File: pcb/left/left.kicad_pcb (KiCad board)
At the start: 2 copper layers, 30.5 x 66 mm, 21 parts

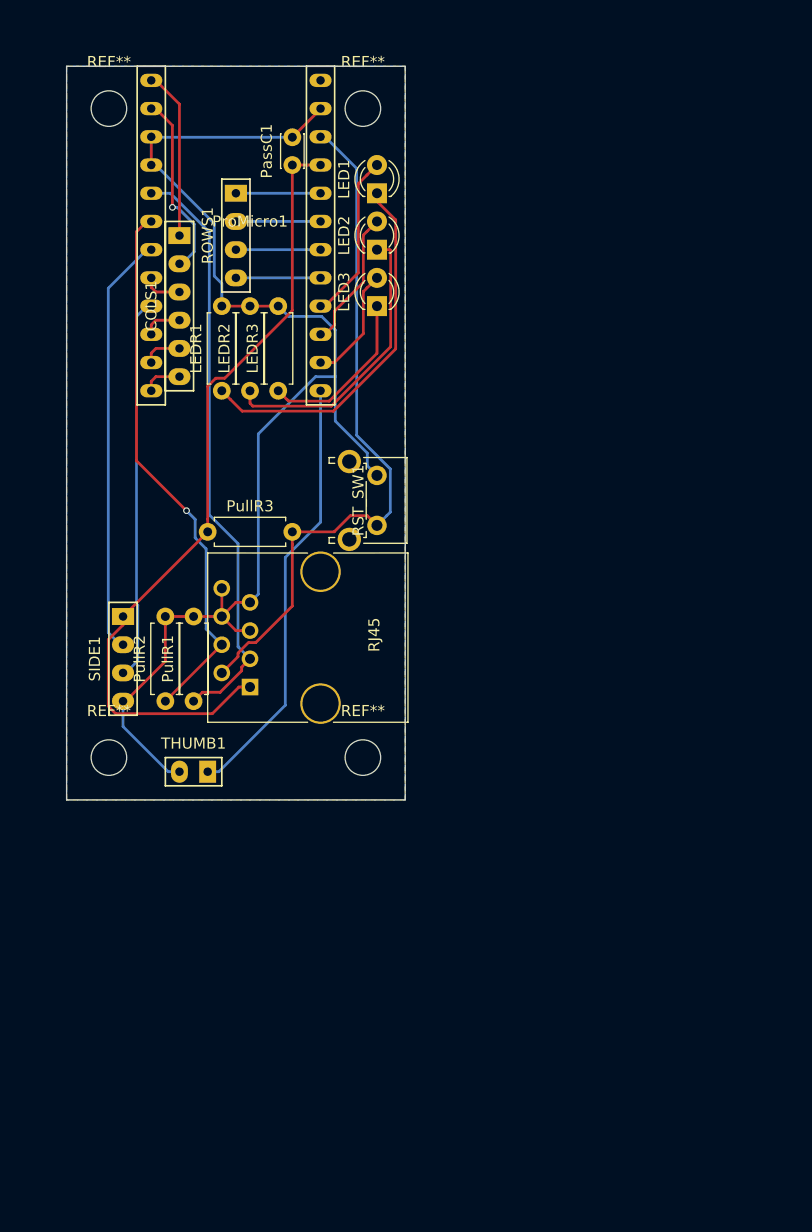
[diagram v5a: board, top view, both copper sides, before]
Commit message: improve parts arrangement
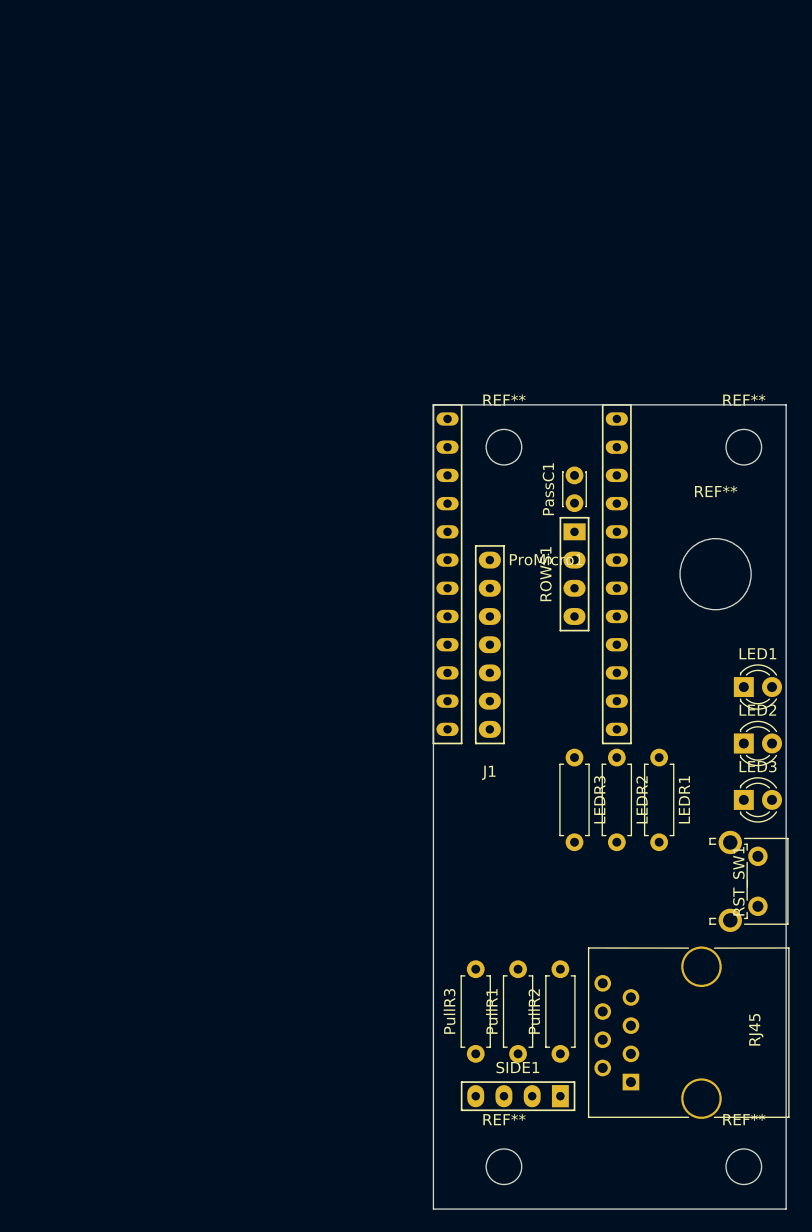
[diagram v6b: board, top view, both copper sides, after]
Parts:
- removed COLS1: Conn_01x06, 4x6t2:Wirepad_01x06
- removed the REF** at (2.54, 2.54)
- removed the REF** at (25.4, 2.54)
- removed the REF** at (2.54, 61.0)
- removed the REF** at (25.4, 61.0)
- removed THUMB1: Conn_01x02, 4x6t2:Wirepad_01x02
- added J1: Conn_01x07, 4x6t2:Wirepad_01x07, F.Cu at (36.8, 57.1)
- added REF**: MountingHole_3.2mm_M3, Mounting_Holes:MountingHole_3.2mm_M3, F.Cu at (59.7, 33.0)
- added REF**: MountingHole_6.4mm_M6, Mounting_Holes:MountingHole_6.4mm_M6, F.Cu at (57.1, 44.5)
- added REF**: MountingHole_3.2mm_M3, Mounting_Holes:MountingHole_3.2mm_M3, F.Cu at (59.7, 97.8)
- added REF**: MountingHole_3.2mm_M3, Mounting_Holes:MountingHole_3.2mm_M3, F.Cu at (38.1, 33.0)
- added REF**: MountingHole_3.2mm_M3, Mounting_Holes:MountingHole_3.2mm_M3, F.Cu at (38.1, 97.8)
- moved LED1 55.4 mm to (59.7, 54.6), turned to 0 degrees
- moved LED2 55.4 mm to (59.7, 59.7), turned to 0 degrees
- moved LED3 55.4 mm to (59.7, 64.8), turned to 0 degrees
- moved SIDE1 53.1 mm to (39.4, 91.4), turned to 270 degrees
- moved PullR3 52.8 mm to (35.6, 87.6), turned to 90 degrees
- moved LEDR1 51.4 mm to (52.1, 61.0), turned to 270 degrees
- moved RJ45 49.4 mm to (49.5, 90.2)
- moved RST_SW1 48.5 mm to (61.0, 69.8)
- moved PullR2 47.7 mm to (43.2, 87.6)
- moved LEDR2 46.7 mm to (48.3, 61.0), turned to 270 degrees
- moved PullR1 43.1 mm to (39.4, 87.6)
- moved ROWS1 43.1 mm to (44.5, 44.5)
- moved LEDR3 42.4 mm to (44.5, 61.0), turned to 270 degrees
- moved ProMicro1 40.5 mm to (41.9, 44.5)
- moved PassC1 39.6 mm to (44.5, 38.1)
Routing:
- net GND: track 116.9 -> 0.00 mm
- net +5V: track 72.6 -> 0.00 mm
- net /RST: track 62.6 -> 0.00 mm
- net /SDA: track 53.5 -> 0.00 mm
- net /SCL: track 49.2 -> 0.00 mm, vias 1 -> 0
- net /Thumb_key: track 39.1 -> 0.00 mm
- net /X: track 38.1 -> 0.00 mm
- net /Y: track 34.5 -> 0.00 mm
- net Net-(LED1-Pad1): track 33.4 -> 0.00 mm
- net Net-(LED2-Pad1): track 26.0 -> 0.00 mm
- net /COL1: track 17.2 -> 0.00 mm, vias 1 -> 0
- net Net-(LED3-Pad1): track 15.3 -> 0.00 mm
- net /COL0: track 15.3 -> 0.00 mm
- net /LED1: track 15.0 -> 0.00 mm
- net /LED2: track 12.5 -> 0.00 mm
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- removed copper zone on B.Cu, net GND
- removed copper zone on F.Cu, net GND
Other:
- board size 30.5 x 66 mm -> 31.8 x 72.4 mm

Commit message: improve pcb size
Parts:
- moved SIDE1 9.92 mm to (47.0, 97.8)
- moved PullR2 3.81 mm to (39.4, 87.6)
- moved RJ45 3.81 mm to (45.7, 90.2)
- moved RST_SW1 3.81 mm to (57.1, 69.8)
- moved LED1 3.81 mm to (55.9, 54.6)
- moved LED2 3.81 mm to (55.9, 59.7)
- moved LED3 3.81 mm to (55.9, 64.8)
- moved REF** 3.81 mm to (55.9, 33.0)
- moved REF** 3.81 mm to (53.3, 44.5)
- moved REF** 3.81 mm to (55.9, 97.8)
- moved PullR1 2.54 mm to (36.8, 87.6)
- moved PullR3 1.27 mm to (34.3, 87.6)
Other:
- board size 31.8 x 72.4 mm -> 27.9 x 72.4 mm
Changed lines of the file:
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@@
     (links 44)
     (no_connects 44)
-    (area 28.539857 27.842 66.710143 103.068)
+    (area 28.539857 27.842 69.250143 103.068)
     (thickness 1.6)
     (drawings 4)
@@
   )
   (module LEDs:LED_D3.0mm (layer F.Cu)
-    (at 59.69 54.61)
+    (at 55.88 54.61)
     (descr "LED, diameter 3.0mm, 2 pins")
     (tags "LED diameter 3.0mm 2 pins")
@@
   )
   (module LEDs:LED_D3.0mm (layer F.Cu)
-    (at 59.69 59.69)
+    (at 55.88 59.69)
     (descr "LED, diameter 3.0mm, 2 pins")
     (tags "LED diameter 3.0mm 2 pins")
@@
   )
   (module LEDs:LED_D3.0mm (layer F.Cu)
-    (at 59.69 64.77)
+    (at 55.88 64.77)
     (descr "LED, diameter 3.0mm, 2 pins")
     (tags "LED diameter 3.0mm 2 pins")
@@
   )
   (module Resistors_THT:R_Axial_DIN0207_L6.3mm_D2.5mm_P7.62mm_Horizontal (layer F.Cu)
-    (at 39.37 87.63 90)
+    (at 36.83 87.63 90)
     (descr "Resistor, Axial_DIN0207 series, Axial, Horizontal, pin pitch=7.62mm, 0.25W = 1/4W, length*diameter=6.3*2.5mm^2, http://cdn-reichelt.de/documents/datenblatt/B400/1_4W%23YAG.pdf")
     (tags "Resistor Axial_DIN0207 series Axial Horizontal pin pitch 7.62mm 0.25W = 1/4W length 6.3mm diameter 2.5mm")
@@
   )
   (module Resistors_THT:R_Axial_DIN0207_L6.3mm_D2.5mm_P7.62mm_Horizontal (layer F.Cu)
-    (at 43.18 87.63 90)
+    (at 39.37 87.63 90)
     (descr "Resistor, Axial_DIN0207 series, Axial, Horizontal, pin pitch=7.62mm, 0.25W = 1/4W, length*diameter=6.3*2.5mm^2, http://cdn-reichelt.de/documents/datenblatt/B400/1_4W%23YAG.pdf")
     (tags "Resistor Axial_DIN0207 series Axial Horizontal pin pitch 7.62mm 0.25W = 1/4W length 6.3mm diameter 2.5mm")
@@
   )
   (module Resistors_THT:R_Axial_DIN0207_L6.3mm_D2.5mm_P7.62mm_Horizontal (layer F.Cu)
-    (at 35.56 87.63 90)
+    (at 34.29 87.63 90)
     (descr "Resistor, Axial_DIN0207 series, Axial, Horizontal, pin pitch=7.62mm, 0.25W = 1/4W, length*diameter=6.3*2.5mm^2, http://cdn-reichelt.de/documents/datenblatt/B400/1_4W%23YAG.pdf")
     (tags "Resistor Axial_DIN0207 series Axial Horizontal pin pitch 7.62mm 0.25W = 1/4W length 6.3mm diameter 2.5mm")
@@
   )
   (module Connectors:RJ45_8 (layer F.Cu)
-    (at 49.53 90.17 90)
+    (at 45.72 90.17 90)
     (tags RJ45)
     (fp_text reference RJ45 (at 4.7 11.18 90) (layer F.SilkS)
@@
   )
   (module Buttons_Switches_THT:SW_Tactile_SPST_Angled_PTS645Vx31-2LFS (layer F.Cu)
-    (at 60.96 69.85 270)
+    (at 57.15 69.85 270)
     (descr "tactile switch SPST right angle, PTS645VL31-2 LFS")
     (tags "tactile switch SPST angled PTS645VL31-2 LFS C&K Button")
@@
   )
   (module 4x6t2:Wirepad_01x04 (layer F.Cu)
-    (at 39.37 91.44 270)
+    (at 46.99 97.79 270)
     (fp_text reference SIDE1 (at -2.54 0 360) (layer F.SilkS)
       (effects (font (size 1 1) (thickness 0.15)))
@@
   )
   (module Mounting_Holes:MountingHole_3.2mm_M3 (layer F.Cu)
-    (at 59.69 33.02)
+    (at 55.88 33.02)
     (descr "Mounting Hole 3.2mm, no annular, M3")
     (tags "mounting hole 3.2mm no annular m3")
@@
   )
   (module Mounting_Holes:MountingHole_6.4mm_M6 (layer F.Cu)
-    (at 57.15 44.45)
+    (at 53.34 44.45)
     (descr "Mounting Hole 6.4mm, no annular, M6")
     (tags "mounting hole 6.4mm no annular m6")
@@
   )
   (module Mounting_Holes:MountingHole_3.2mm_M3 (layer F.Cu)
-    (at 59.69 97.79)
+    (at 55.88 97.79)
     (descr "Mounting Hole 3.2mm, no annular, M3")
     (tags "mounting hole 3.2mm no annular m3")
@@
       (net 6 /COL5))
   )
-  (gr_line (start 31.75 101.6) (end 63.5 101.6) (layer Edge.Cuts) (width 0.1))
-  (gr_line (start 63.5 29.21) (end 63.5 101.6) (layer Edge.Cuts) (width 0.1))
+  (gr_line (start 31.75 101.6) (end 59.69 101.6) (layer Edge.Cuts) (width 0.1))
+  (gr_line (start 59.69 29.21) (end 59.69 101.6) (layer Edge.Cuts) (width 0.1))
   (gr_line (start 31.75 29.21) (end 31.75 101.6) (layer Edge.Cuts) (width 0.1))
-  (gr_line (start 63.5 29.21) (end 31.75 29.21) (layer Edge.Cuts) (width 0.1))
+  (gr_line (start 59.69 29.21) (end 31.75 29.21) (layer Edge.Cuts) (width 0.1))
 )

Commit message: connect pad
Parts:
- moved LEDR1 10.8 mm to (44.5, 68.6), turned to 90 degrees
- moved LEDR3 10.8 mm to (52.1, 68.6), turned to 90 degrees
- moved LEDR2 7.62 mm to (48.3, 68.6), turned to 90 degrees
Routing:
- net GND: track 0.00 -> 137.9 mm
- net +5V: track 0.00 -> 93.6 mm
- net /RST: track 0.00 -> 83.6 mm, vias 0 -> 1
- net /X: track 0.00 -> 62.9 mm
- net /Y: track 0.00 -> 61.8 mm, vias 0 -> 1
- net /SDA: track 0.00 -> 59.6 mm
- net /SCL: track 0.00 -> 55.1 mm
- net /Thumb_key: track 0.00 -> 20.3 mm
- net Net-(LED1-Pad1): track 0.00 -> 19.7 mm
- net /COL1: track 0.00 -> 17.2 mm
- net /COL0: track 0.00 -> 17.0 mm
- net /LED3: track 0.00 -> 13.8 mm
- net /LED2: track 0.00 -> 12.8 mm
- net Net-(LED2-Pad1): track 0.00 -> 12.0 mm
- net /LED1: track 0.00 -> 11.7 mm
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- added copper zone on B.Cu, net GND
- added copper zone on F.Cu, net GND
